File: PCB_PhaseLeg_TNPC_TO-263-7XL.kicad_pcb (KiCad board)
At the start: 2 copper layers, 88 x 86.8 mm, 4 parts, among them Q1 C3M0075120J, Q2 C3M0075120J, Q3 C3M0075120J, Q4 C3M0075120J

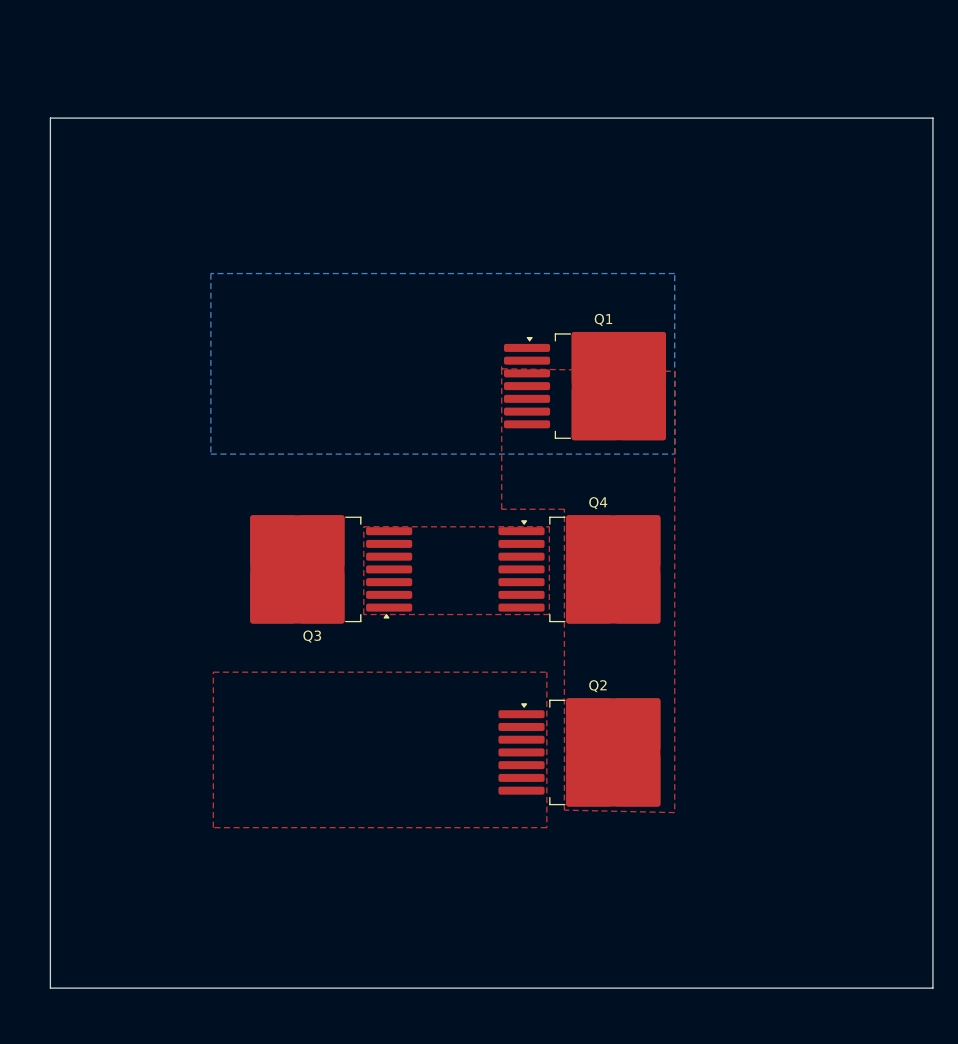
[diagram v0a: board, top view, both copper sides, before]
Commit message: pcb heatsink
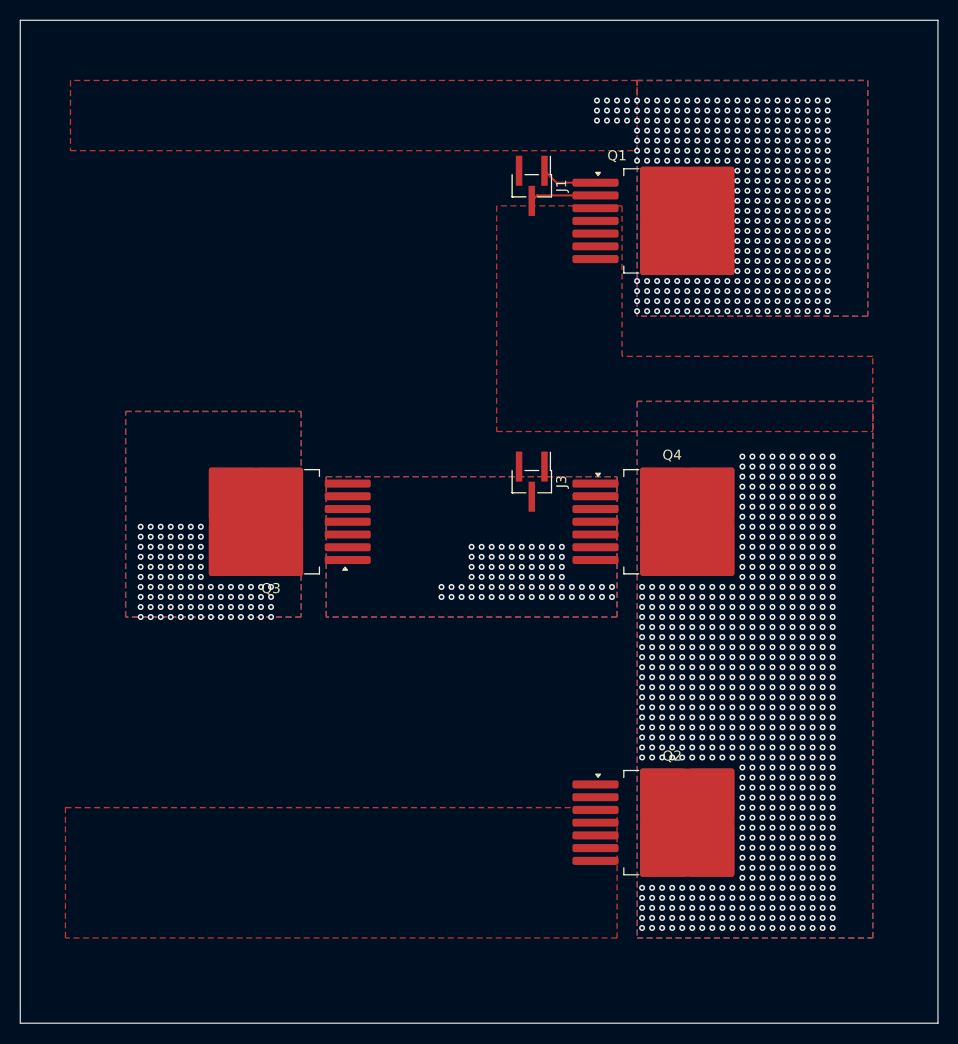
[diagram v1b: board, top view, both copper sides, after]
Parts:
- added J1: Conn_01x03, Connector_PinHeader_1.27mm:PinHeader_1x03_P1.27mm_Vertical_SMD_Pin1Left, F.Cu at (106.0, 51.5)
- added J3: Conn_01x03, Connector_PinHeader_1.27mm:PinHeader_1x03_P1.27mm_Vertical_SMD_Pin1Left, F.Cu at (106.0, 81.0)
- moved Q1 17.8 mm to (120.0, 55.0)
- moved Q2 10.2 mm to (120.0, 115.0)
- moved Q4 8.77 mm to (120.0, 85.0)
- moved Q3 6.29 mm to (80.0, 85.0)
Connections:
- Q1 pad 1: unconnected-(Q1-G-Pad1) -> /g1
- Q1 pad 2: unconnected-(Q1-DS-Pad2) -> /ks1
- Q4 pad 1: unconnected-(Q4-G-Pad1) -> /g3
- Q4 pad 2: unconnected-(Q4-DS-Pad2) -> /ks3
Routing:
- net /ks1: track 0.00 -> 6.57 mm
- net /g1: track 0.00 -> 5.57 mm
- net /vccp: vias 0 -> 342
- net /vccm: vias 0 -> 98
- net /ph: vias 0 -> 710
- net /ce: vias 0 -> 76
- added copper zone on B.Cu, net /ce
- added copper zone on B.Cu, net /ph
- added copper zone on B.Cu, net /vccm
- added copper zone on F.Cu, net /vccm
- added copper zone on F.Cu, net /vccp
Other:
- board size 88 x 86.8 mm -> 91.5 x 100 mm
